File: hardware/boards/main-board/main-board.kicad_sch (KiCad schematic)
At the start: 15 parts, among them J4 12-way, J5 12-way, J6 8-way 2.54mm right-angle pin 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, U10 MPXV4006DP, U9 SP0504BAHTG 4-channel 5V array

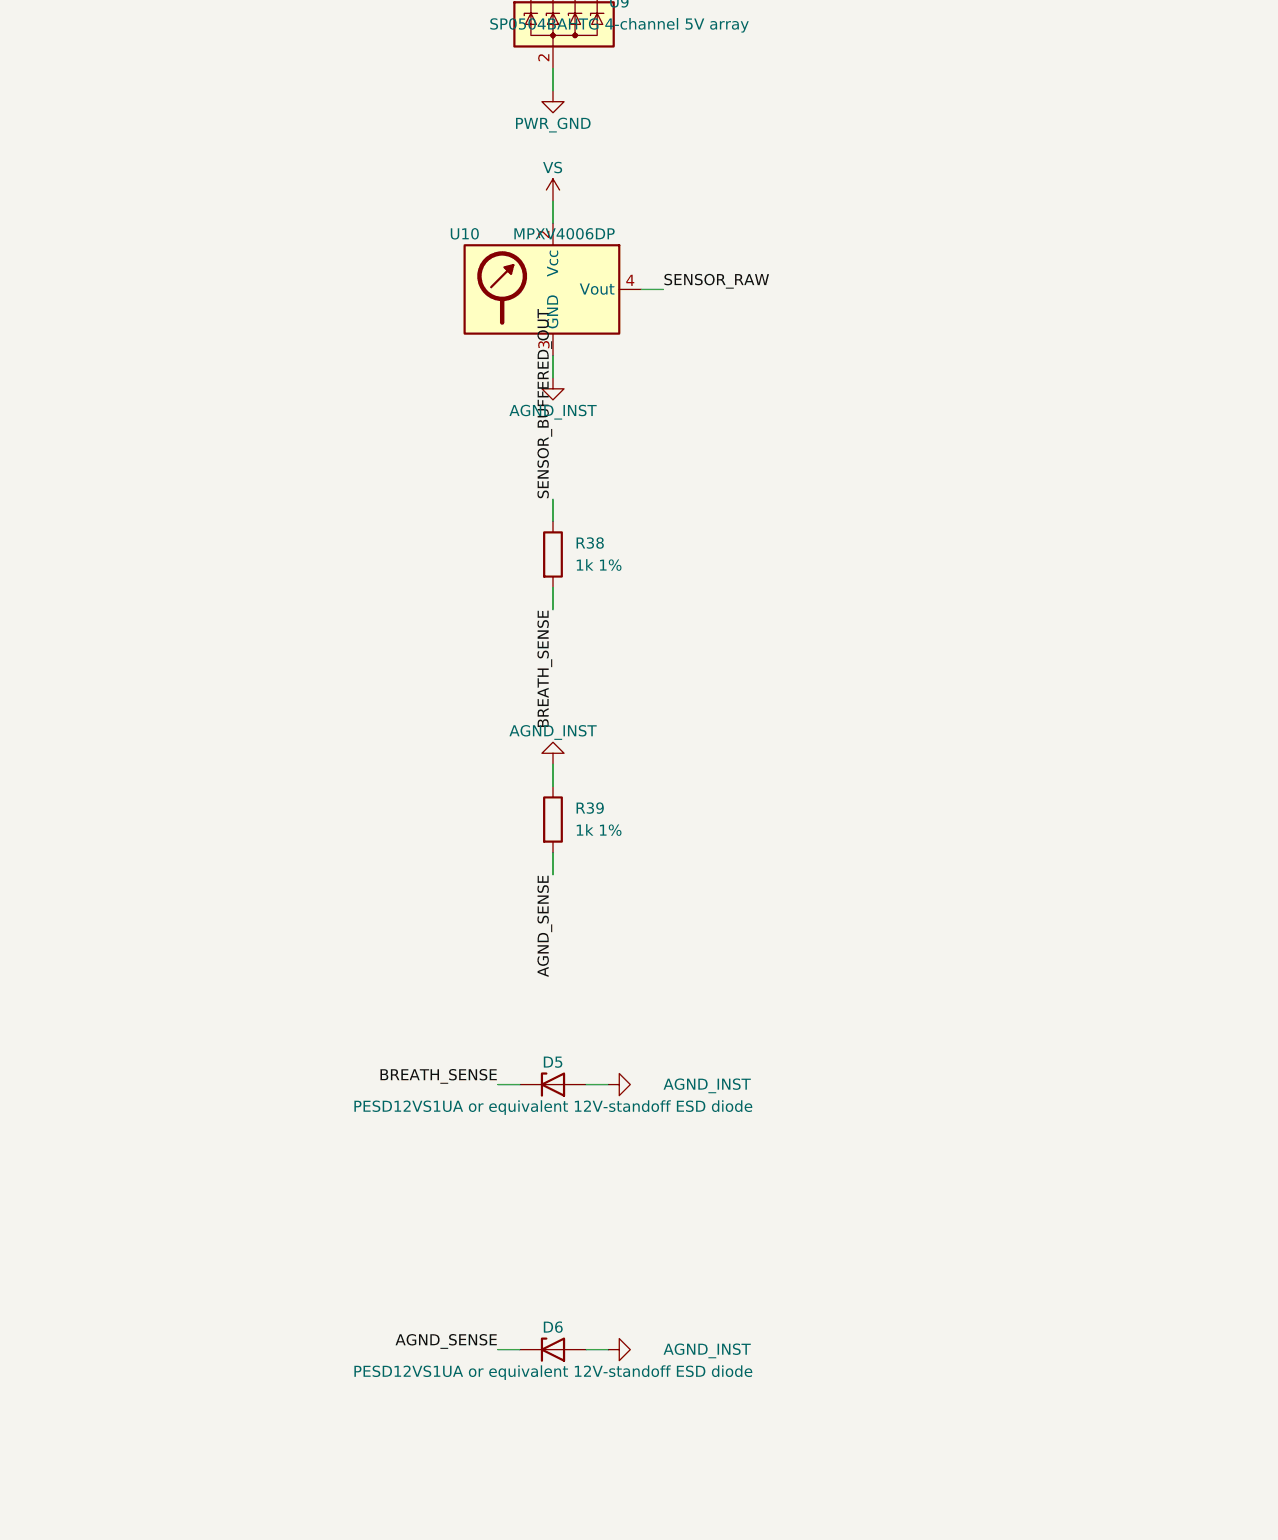
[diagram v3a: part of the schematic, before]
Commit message: Main board places the breath-sense-link sheet; AGND_SENSE taken at the sensor pin; AN3150 recorded BLOCKED
The five root-sheet parts (U10, R38, R39, D5, D6) are now one placement of
interfaces/breath-sense-link, same references; board-netlist.yaml compared
before and after, net by net: unchanged. AGND_SENSE is Kelvin-taken at
U-BREATH pin 3 (a layout rule, same net). AN3150 could not be fetched:
datasheets/.manifest-R32.csv records the URLs.

Co-Authored-By: Claude Opus 5.5 <noreply@anthropic.com>
Claude-Session: https://claude.ai/code/session_01LmB4muFXnoLprWX4JzuJ5A
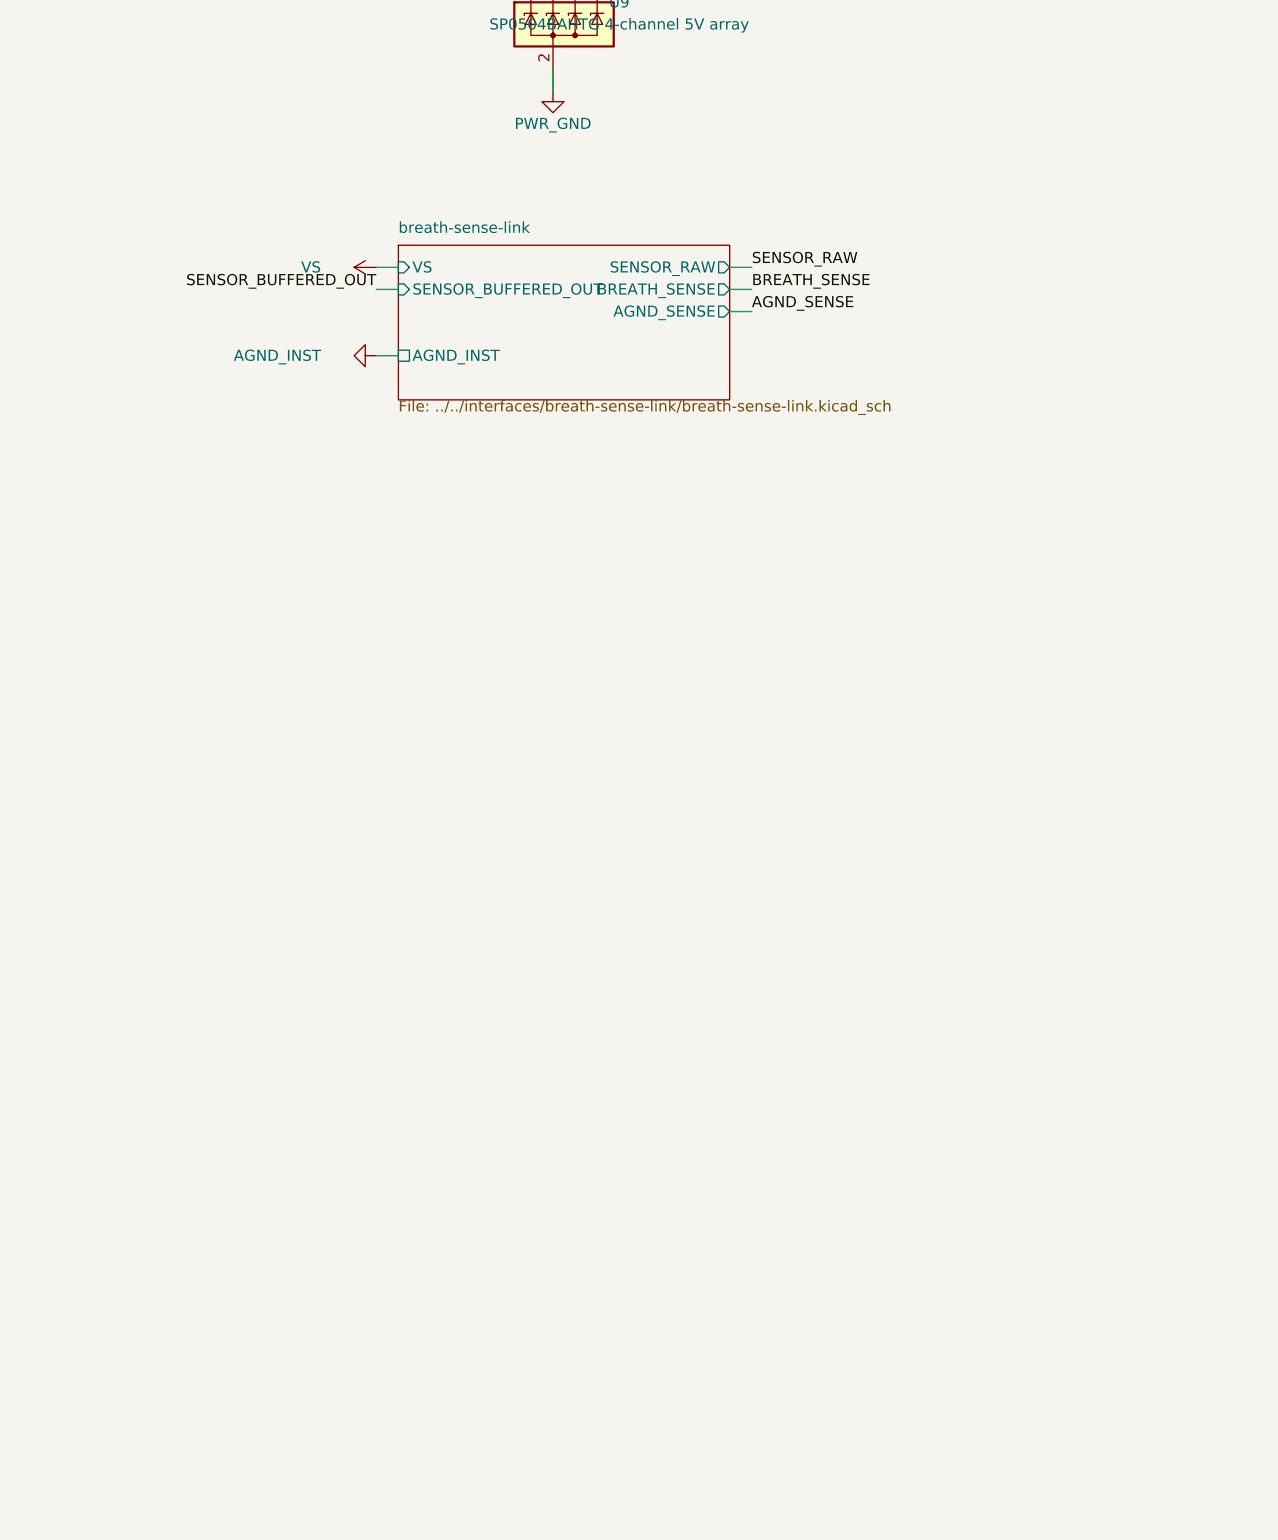
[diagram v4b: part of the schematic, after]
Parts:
- removed D5, D6: PESD12VS1UA or equivalent 12V-standoff ESD diode, Diode_SMD:D_SOD-323, symbol Device:D_Zener
- removed R38, R39: 1k 1%, Resistor_SMD:R_1206_3216Metric, symbol Device:R
- removed U10: MPXV4006DP, woody:NXP_Case1351-01_SOP-8_P2.54mm, symbol Sensor_Pressure:MPXA6115A
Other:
- added sheet breath-sense-link (../../interfaces/breath-sense-link/breath-sense-link.kicad_sch)

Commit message: Four-layer main-board ground written; breath clamps to the PWR_GND plane
power-entry-instrument.md section 2: layer 2 is the PWR_GND plane under every
SPI/chain/LED trace; AGND_INST is an island under the analog block, tied by
NT-AGND under U-ADC; the breath pair crosses as a pair (AGND_SENSE Kelvin at
the sensor). D-TVS-BREATH anodes move from AGND_INST to PWR_GND (sheet, board,
nets.yaml). dig-gnd-topology stays disputed: its dispute is the MODULE board,
whose layer count is the owner's; a four-layer proposal is recorded on it.

Co-Authored-By: Claude Opus 5.5 <noreply@anthropic.com>
Claude-Session: https://claude.ai/code/session_01LmB4muFXnoLprWX4JzuJ5A
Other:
- sheet breath-sense-link ports: added PWR_GND; removed none
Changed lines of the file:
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@@
     (pin "VS" input (at 88.9 363.22 180) (effects (font (size 1.27 1.27)) (justify left)))
     (pin "SENSOR_BUFFERED_OUT" input (at 88.9 365.76 180) (effects (font (size 1.27 1.27)) (justify left)))
+    (pin "PWR_GND" passive (at 88.9 375.92 180) (effects (font (size 1.27 1.27)) (justify left)))
     (pin "AGND_INST" passive (at 88.9 373.38 180) (effects (font (size 1.27 1.27)) (justify left)))
     (pin "SENSOR_RAW" output (at 127.0 363.22 0) (effects (font (size 1.27 1.27)) (justify right)))
@@
   (wire (pts (xy 127.00 368.30) (xy 129.54 368.30)) (stroke (width 0) (type default)))
   (label "AGND_SENSE" (at 129.54 368.30 0) (fields_autoplaced) (effects (font (size 1.27 1.27)) (justify left bottom)))
+  (wire (pts (xy 88.90 375.92) (xy 86.36 375.92)) (stroke (width 0) (type default)))
+  (symbol (lib_id "power:GND") (at 86.36 375.92 270) (unit 1)
+    (in_bom yes) (on_board yes) (dnp no)
+    (property "Reference" "#PWR54" (at 86.36 375.92 0) (effects (font (size 1.27 1.27)) hide))
+    (property "Value" "PWR_GND" (at 80.01 375.92 270) (effects (font (size 1.27 1.27)) (justify left)))
+    (property "Footprint" "" (at 86.36 375.92 0) (effects (font (size 1.27 1.27)) hide))
+    (property "Datasheet" "" (at 86.36 375.92 0) (effects (font (size 1.27 1.27)) hide))
+    (pin "1")
+    (instances (project "main-board" (path "/b12a49ac-ffa0-5078-b2ba-e15d161f1936" (reference "#PWR54") (unit 1))))
+  )
   (sheet_instances (path "/" (page "1")))
 )

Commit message: Main board footprints from the banked drawings: J-MCU, J-UMB drawn; models on J-CHAIN and U-BREATH; LED chamfer mark
J-MCU (XKB X1270WR-2x12A-9TV01): 0.70 holes, 1.50 x 1.07 pads with the
hole off centre (the J-CHAIN pattern, JLC's 0.18 ring), the tail rows
2.60 and 1.33 behind the body per the drawing's rev A1 side view.
J-UMB (HX PZ2.54-1x8P WZ): 1.02 holes, insulator 1.80 in front of the row.
U-BREATH: courtyard takes in the ports. WS2815B-V1: filled silk
triangle at the chamfer (pin 4).

Co-Authored-By: Claude Opus 5.5 <noreply@anthropic.com>
Claude-Session: https://claude.ai/code/session_01LmB4muFXnoLprWX4JzuJ5A
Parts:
- J6: footprint Connector_PinHeader_2.54mm:PinHeader_1x08_P2.54mm_Horizontal -> woody:PinHeader_1x08_P2.54mm_Horizontal_Hanxia_PZ2.54-WZ
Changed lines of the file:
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@@
     (property "Reference" "J6" (at 106.68 520.7 0) (effects (font (size 1.27 1.27))))
     (property "Value" "8-way 2.54mm right-angle pin header" (at 106.68 543.56 0) (effects (font (size 1.27 1.27))))
-    (property "Footprint" "Connector_PinHeader_2.54mm:PinHeader_1x08_P2.54mm_Horizontal" (at 106.68 530.86 0) (effects (font (size 1.27 1.27)) hide))
+    (property "Footprint" "woody:PinHeader_1x08_P2.54mm_Horizontal_Hanxia_PZ2.54-WZ" (at 106.68 530.86 0) (effects (font (size 1.27 1.27)) hide))
     (property "Datasheet" "" (at 106.68 530.86 0) (effects (font (size 1.27 1.27)) hide))
     (property "Row" "J-UMB" (at 106.68 530.86 0) (effects (font (size 1.27 1.27)) hide))
